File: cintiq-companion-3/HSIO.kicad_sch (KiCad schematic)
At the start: 25 parts, among them J3 Bus_M.2_Socket_M, J4 Bus_M.2_Socket_E, J5 Bus_M.2_Socket_B, J6 USB3_A

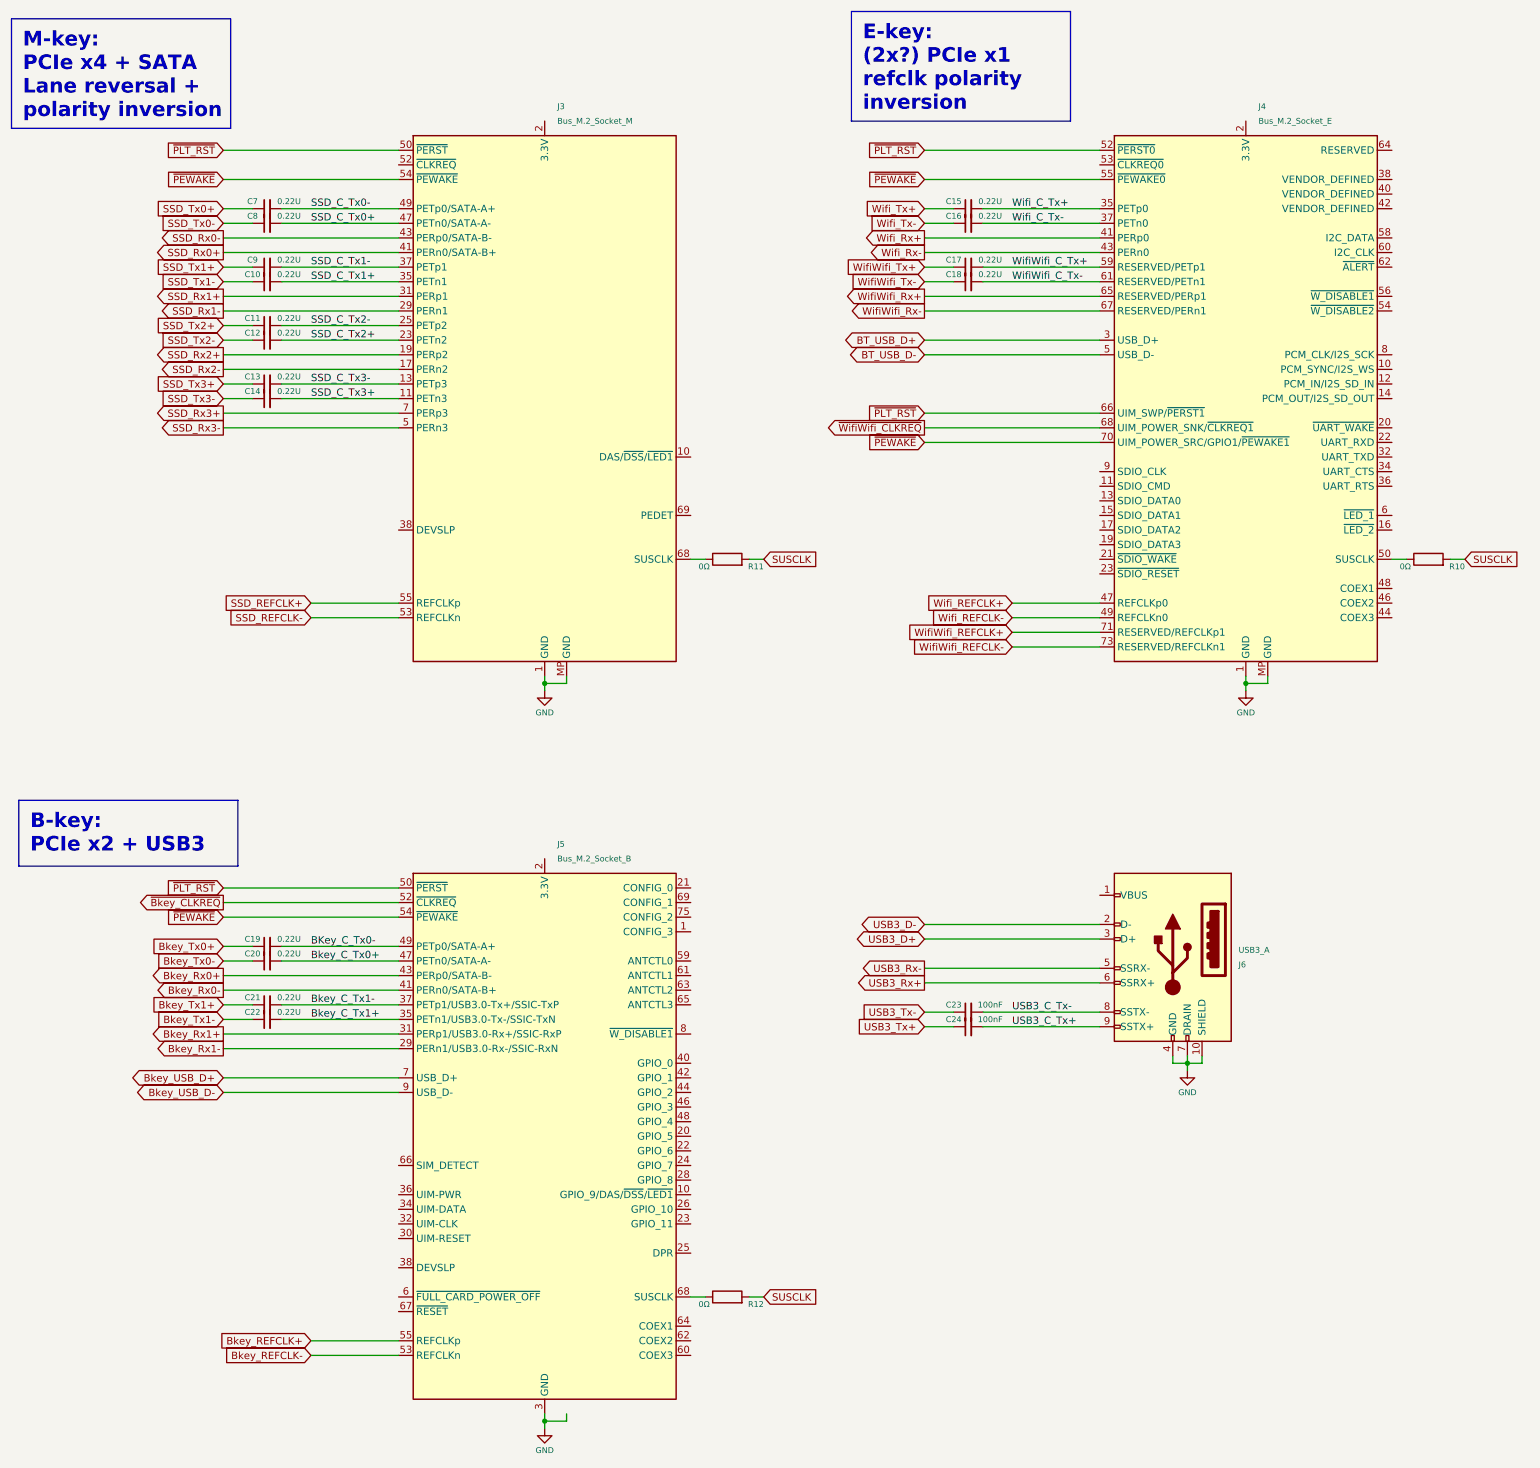
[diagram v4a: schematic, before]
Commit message: unflipped m-key polarity for sata
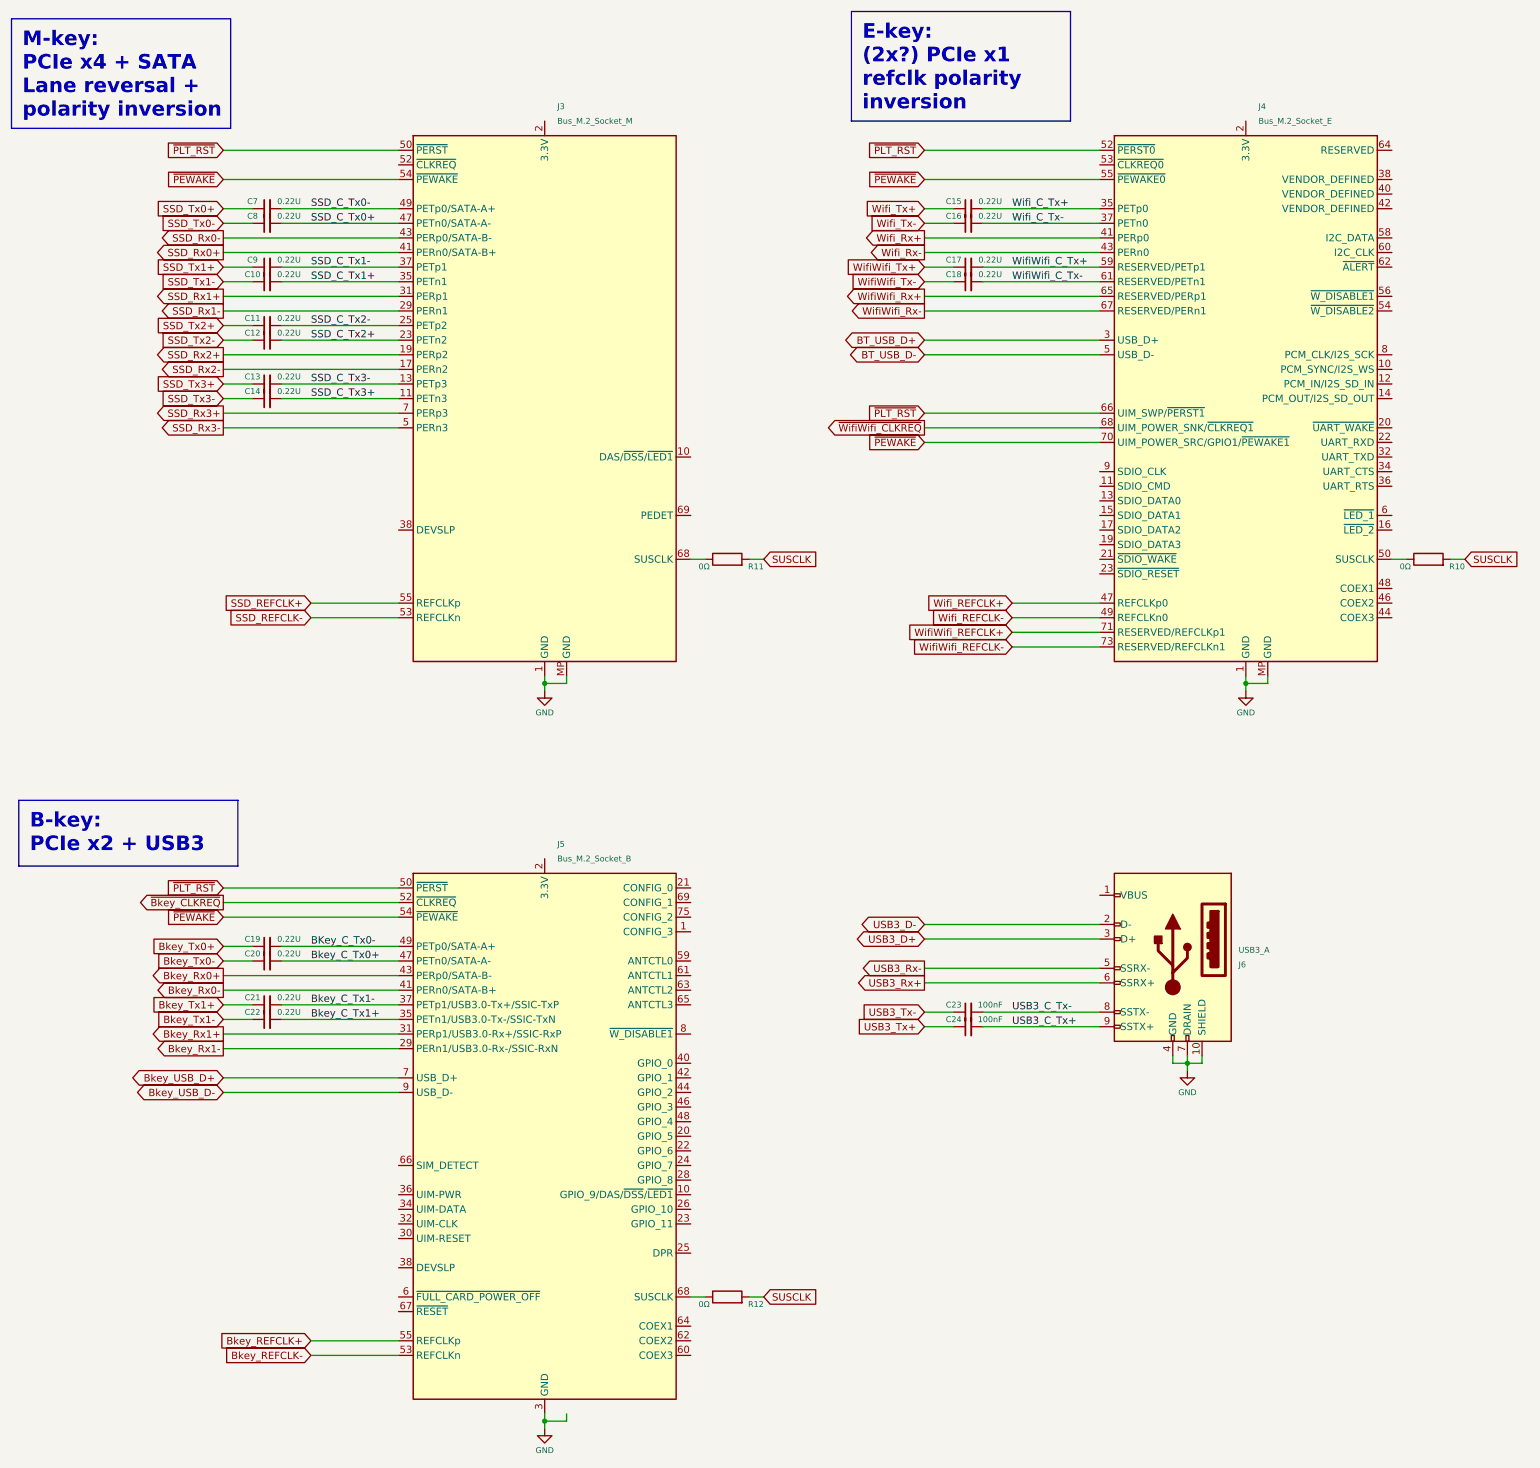
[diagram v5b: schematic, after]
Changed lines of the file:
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@@
 (kicad_sch
-	(version 20231120)
+	(version 20250114)
 	(generator "eeschema")
-	(generator_version "8.0")
+	(generator_version "9.0")
 	(paper "A3")
+	(text_box "B-key:\nPCIe x2 + USB3"
+		(exclude_from_sim no)
+		(at 17.78 160.02 0)
+		(size 38.1 11.43)
+		(margins 1.905 1.905 1.905 1.905)
+		(stroke
+			(width 0)
+			(type default)
+		)
+		(fill
+			(type none)
+		)
+		(effects
+			(font
+				(size 2.54 2.54)
+				(thickness 0.508)
+				(bold yes)
+			)
+			(justify left top)
+		)
+	)
+	(text_box "E-key:\n(2x?) PCIe x1\nrefclk polarity inversion"
+		(exclude_from_sim no)
+		(at 162.56 22.86 0)
+		(size 38.1 19.05)
+		(margins 1.905 1.905 1.905 1.905)
+		(stroke
+			(width 0)
+			(type default)
+		)
+		(fill
+			(type none)
+		)
+		(effects
+			(font
+				(size 2.54 2.54)
+				(thickness 0.508)
+				(bold yes)
+			)
+			(justify left top)
+		)
+	)
+	(text_box "M-key:\nPCIe x4 + SATA\nLane reversal +\npolarity inversion"
+		(exclude_from_sim no)
+		(at 16.51 24.13 0)
+		(size 38.1 19.05)
+		(margins 1.905 1.905 1.905 1.905)
+		(stroke
+			(width 0)
+			(type default)
+		)
+		(fill
+			(type none)
+		)
+		(effects
+			(font
+				(size 2.54 2.54)
+				(thickness 0.508)
+				(bold yes)
+			)
+			(justify left top)
+		)
+	)
 	(junction
 		(at 109.22 139.7)
@@
 		)
 	)
-	(text_box "B-key:\nPCIe x2 + USB3"
-		(exclude_from_sim no)
-		(at 17.78 160.02 0)
-		(size 38.1 11.43)
-		(stroke
-			(width 0)
-			(type default)
-		)
-		(fill
-			(type none)
-		)
-		(effects
-			(font
-				(size 2.54 2.54)
-				(thickness 0.508)
-				(bold yes)
-			)
-			(justify left top)
-		)
-	)
-	(text_box "E-key:\n(2x?) PCIe x1\nrefclk polarity inversion"
-		(exclude_from_sim no)
-		(at 162.56 22.86 0)
-		(size 38.1 19.05)
-		(stroke
-			(width 0)
-			(type default)
-		)
-		(fill
-			(type none)
-		)
-		(effects
-			(font
-				(size 2.54 2.54)
-				(thickness 0.508)
-				(bold yes)
-			)
-			(justify left top)
-		)
-	)
-	(text_box "M-key:\nPCIe x4 + SATA\nLane reversal +\npolarity inversion"
-		(exclude_from_sim no)
-		(at 16.51 24.13 0)
-		(size 38.1 19.05)
-		(stroke
-			(width 0)
-			(type default)
-		)
-		(fill
-			(type none)
-		)
-		(effects
-			(font
-				(size 2.54 2.54)
-				(thickness 0.508)
-				(bold yes)
-			)
-			(justify left top)
-		)
-	)
 	(label "SSD_C_Tx2+"
 		(at 68.58 80.01 0)
-		(fields_autoplaced yes)
 		(effects
 			(font
@@
 	(label "Wifi_C_Tx-"
 		(at 190.5 59.69 0)
-		(fields_autoplaced yes)
 		(effects
 			(font
@@
 	(label "SSD_C_Tx3+"
 		(at 68.58 90.17 0)
-		(fields_autoplaced yes)
 		(effects
 			(font
@@
 	(label "Wifi_C_Tx+"
 		(at 190.5 57.15 0)
-		(fields_autoplaced yes)
 		(effects
 			(font
@@
 	(label "BKey_C_Tx0-"
 		(at 68.58 185.42 0)
-		(fields_autoplaced yes)
 		(effects
 			(font
@@
 	(label "SSD_C_Tx1-"
 		(at 68.58 67.31 0)
-		(fields_autoplaced yes)
 		(effects
 			(font
@@
 	(label "USB3_C_Tx+"
 		(at 190.5 199.39 0)
-		(fields_autoplaced yes)
 		(effects
 			(font
@@
 	(label "SSD_C_Tx3-"
 		(at 68.58 87.63 0)
-		(fields_autoplaced yes)
 		(effects
 			(font
@@
 	(label "SSD_C_Tx1+"
 		(at 68.58 69.85 0)
-		(fields_autoplaced yes)
 		(effects
 			(font
@@
 	(label "WifiWifi_C_Tx-"
 		(at 190.5 69.85 0)
-		(fields_autoplaced yes)
 		(effects
 			(font
@@
 	(label "Bkey_C_Tx1-"
 		(at 68.58 195.58 0)
-		(fields_autoplaced yes)
 		(effects
 			(font
@@
 	(label "Bkey_C_Tx1+"
 		(at 68.58 198.12 0)
-		(fields_autoplaced yes)
 		(effects
 			(font
@@
 	(label "Bkey_C_Tx0+"
 		(at 68.58 187.96 0)
-		(fields_autoplaced yes)
 		(effects
 			(font
@@
 	(label "USB3_C_Tx-"
 		(at 190.5 196.85 0)
-		(fields_autoplaced yes)
 		(effects
 			(font
@@
 	(label "WifiWifi_C_Tx+"
 		(at 190.5 67.31 0)
-		(fields_autoplaced yes)
 		(effects
 			(font
@@
 	(label "SSD_C_Tx0-"
 		(at 68.58 57.15 0)
-		(fields_autoplaced yes)
 		(effects
 			(font
@@
 	(label "SSD_C_Tx2-"
 		(at 68.58 77.47 0)
-		(fields_autoplaced yes)
 		(effects
 			(font
@@
 	(label "SSD_C_Tx0+"
 		(at 68.58 59.69 0)
-		(fields_autoplaced yes)
-		(effects
-			(font
+		(effects
+			(font
